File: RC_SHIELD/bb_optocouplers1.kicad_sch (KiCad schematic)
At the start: 40 parts, among them U1 SFH6345, U2 SFH6345, U6 SFH6345, U8 SFH6345

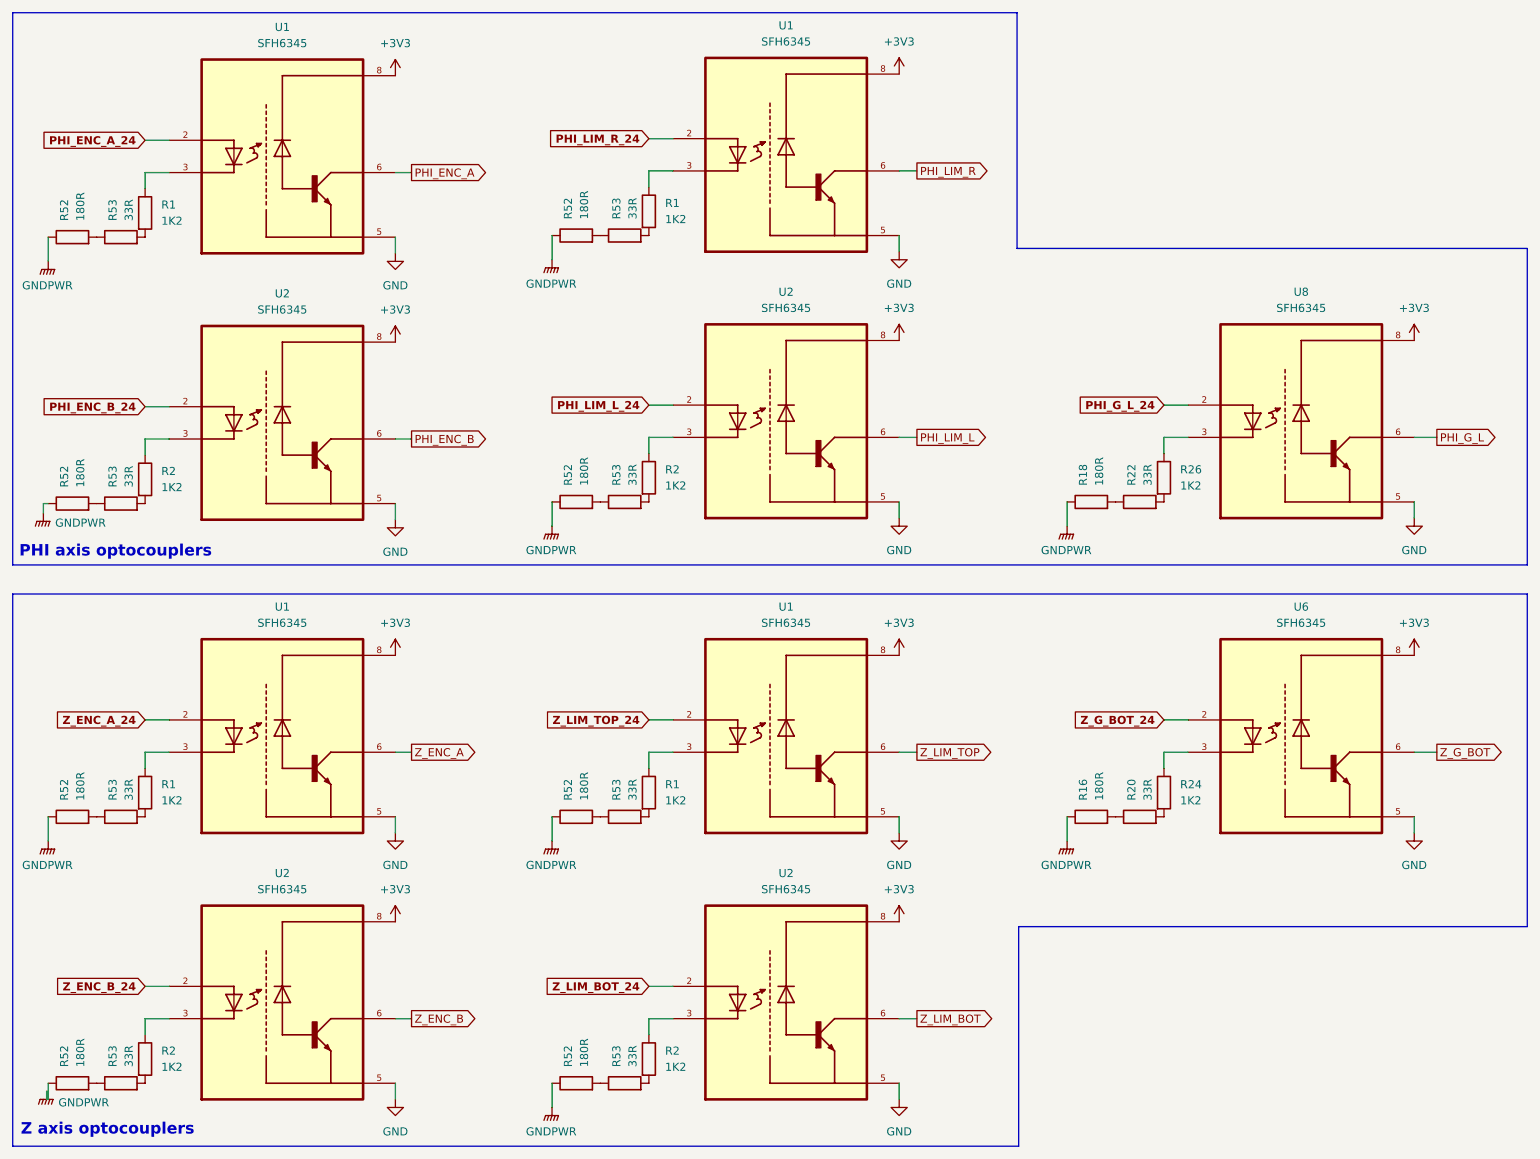
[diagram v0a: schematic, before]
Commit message: [SCH] reorganized optocouplers and tidied up page 2
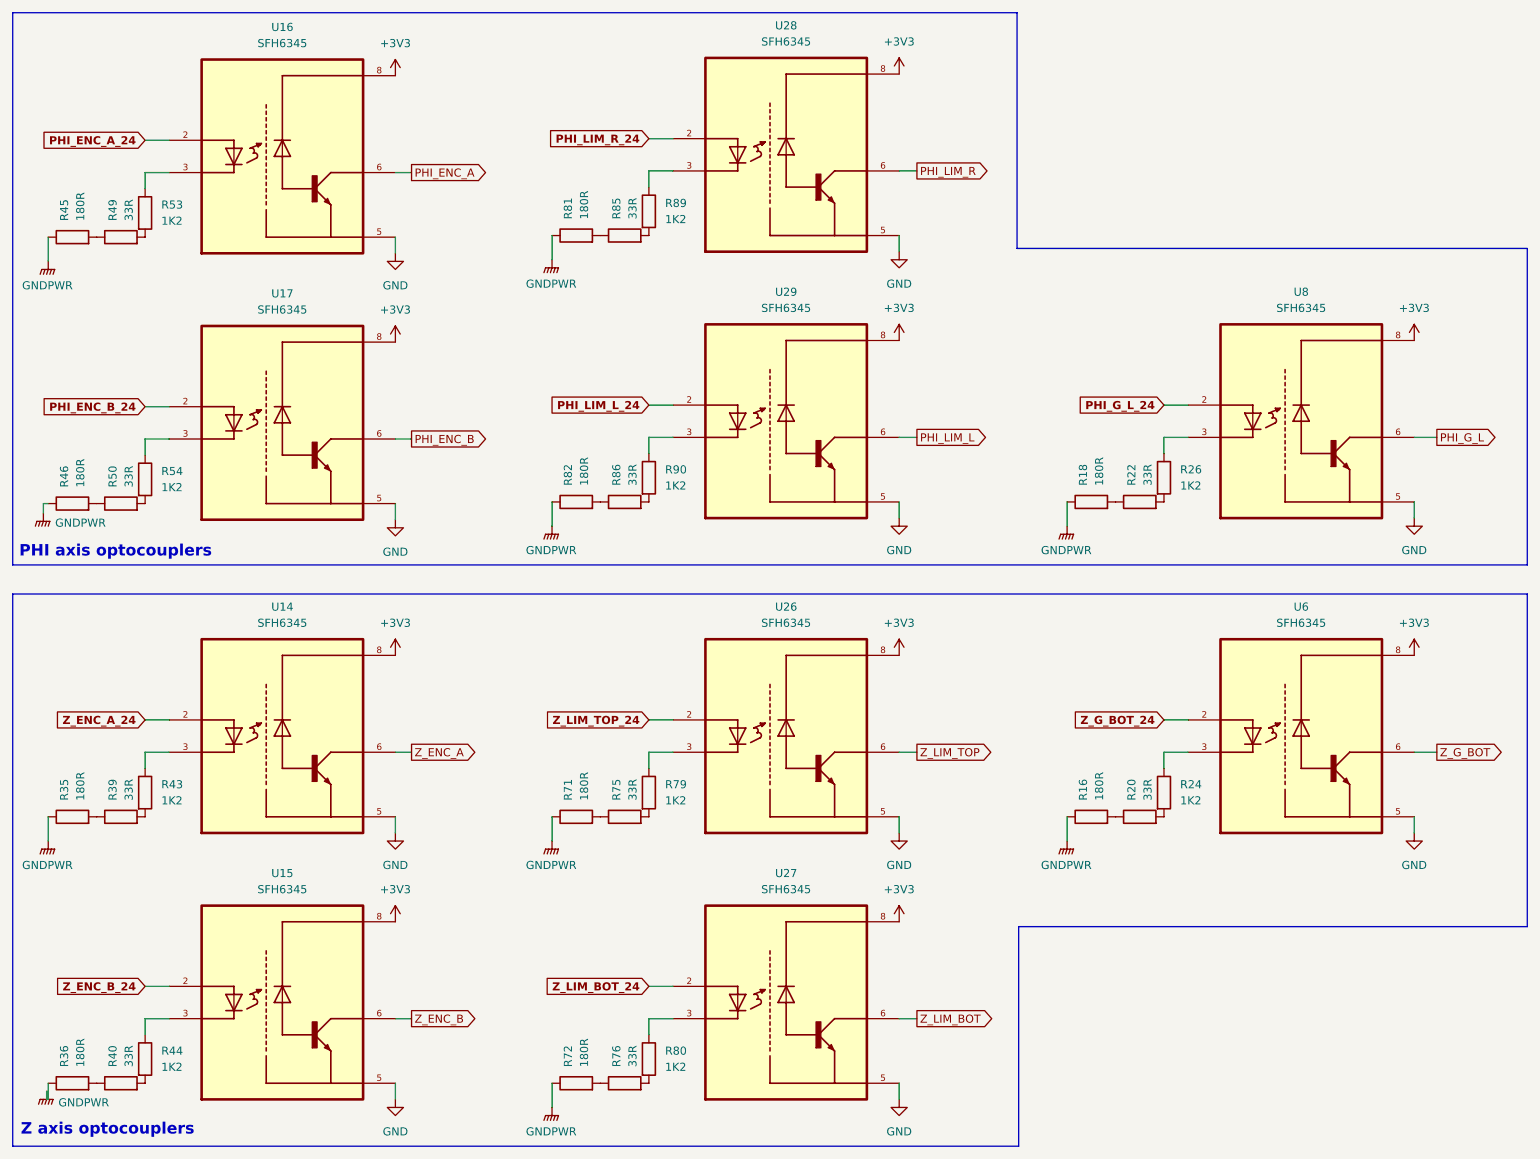
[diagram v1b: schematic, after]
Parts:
- renumbered R52 to R35, R52 to R36, R53 to R39, R53 to R40, R1 to R43, R2 to R44, R52 to R45, R52 to R46, R53 to R49, R53 to R50, R1 to R53, R2 to R54, R52 to R71, R52 to R72, R53 to R75, R53 to R76, R1 to R79, R2 to R80, R52 to R81, R52 to R82, R53 to R85, R53 to R86, R1 to R89, R2 to R90, U1 to U14, U2 to U15, U1 to U16, U2 to U17, U1 to U26, U2 to U27, U1 to U28, U2 to U29

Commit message: [SCH] reannotated entire schematic so PCBnew wont complain
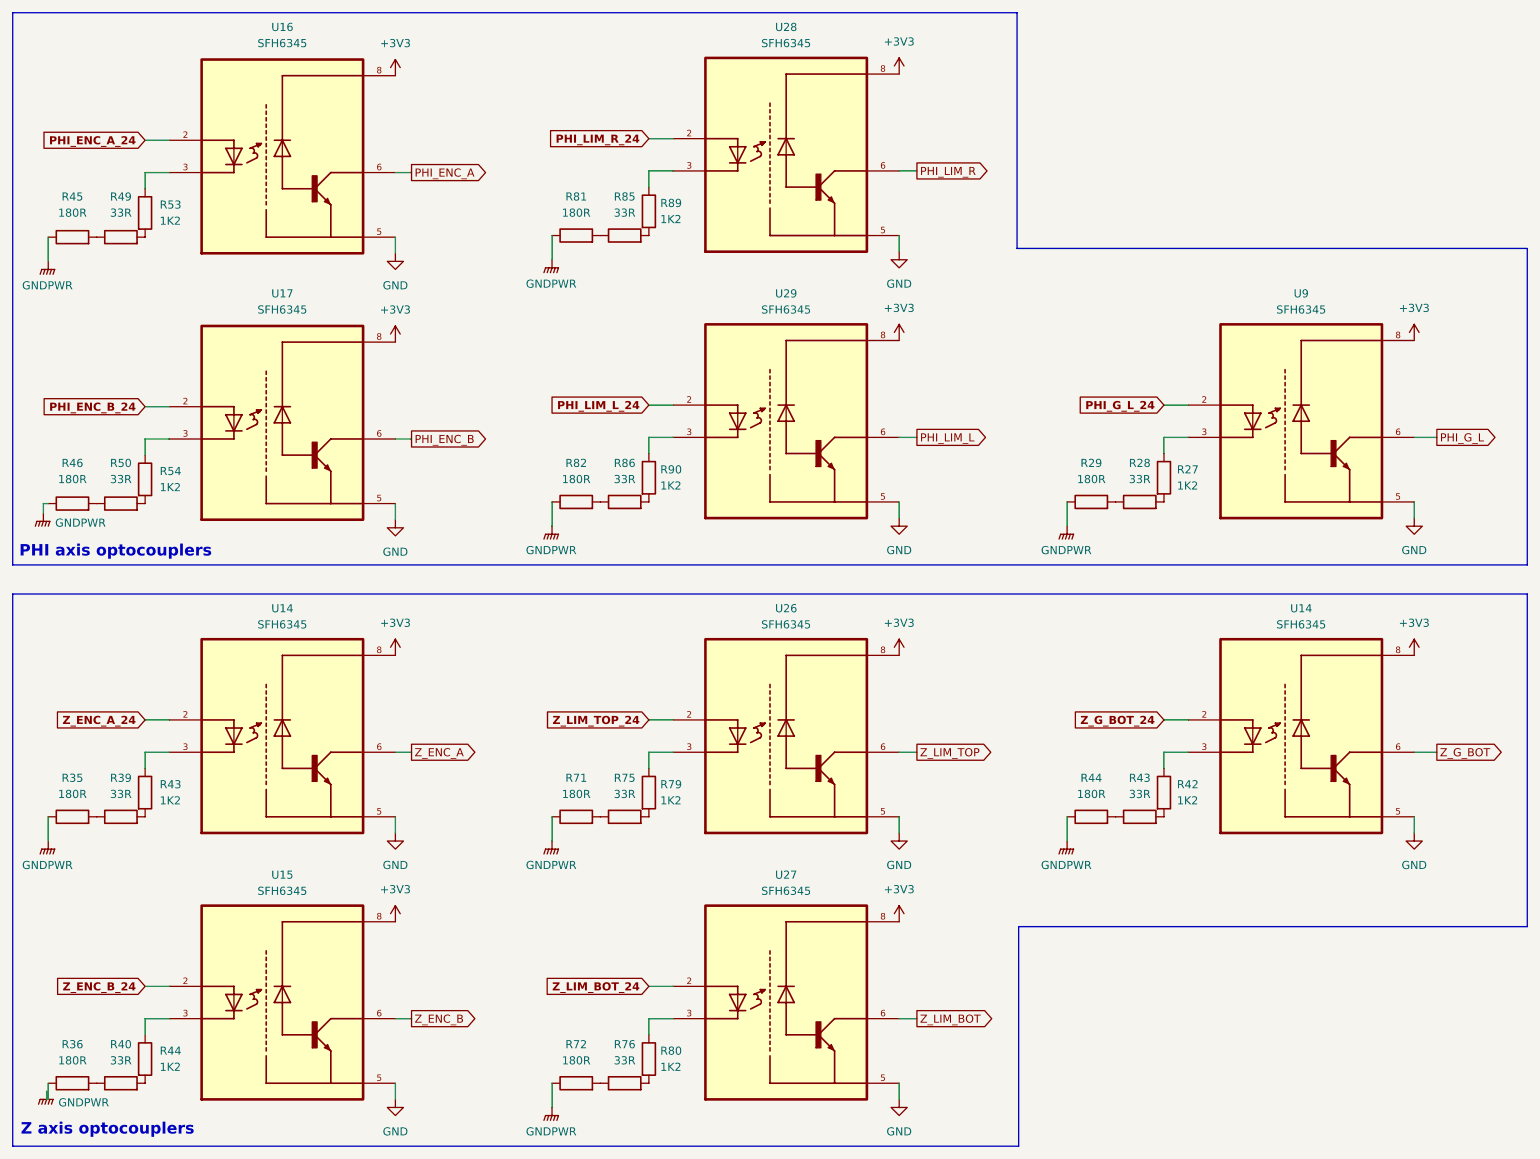
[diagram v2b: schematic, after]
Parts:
- renumbered R26 to R27, R22 to R28, R18 to R29, R24 to R42, R20 to R43, R16 to R44, U6 to U14, U8 to U9

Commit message: Revert "[SCH] reannotated entire schematic so PCBnew wont complain"
This reverts commit df148950bb8496d2d5af5a937770664cb0004a0d.
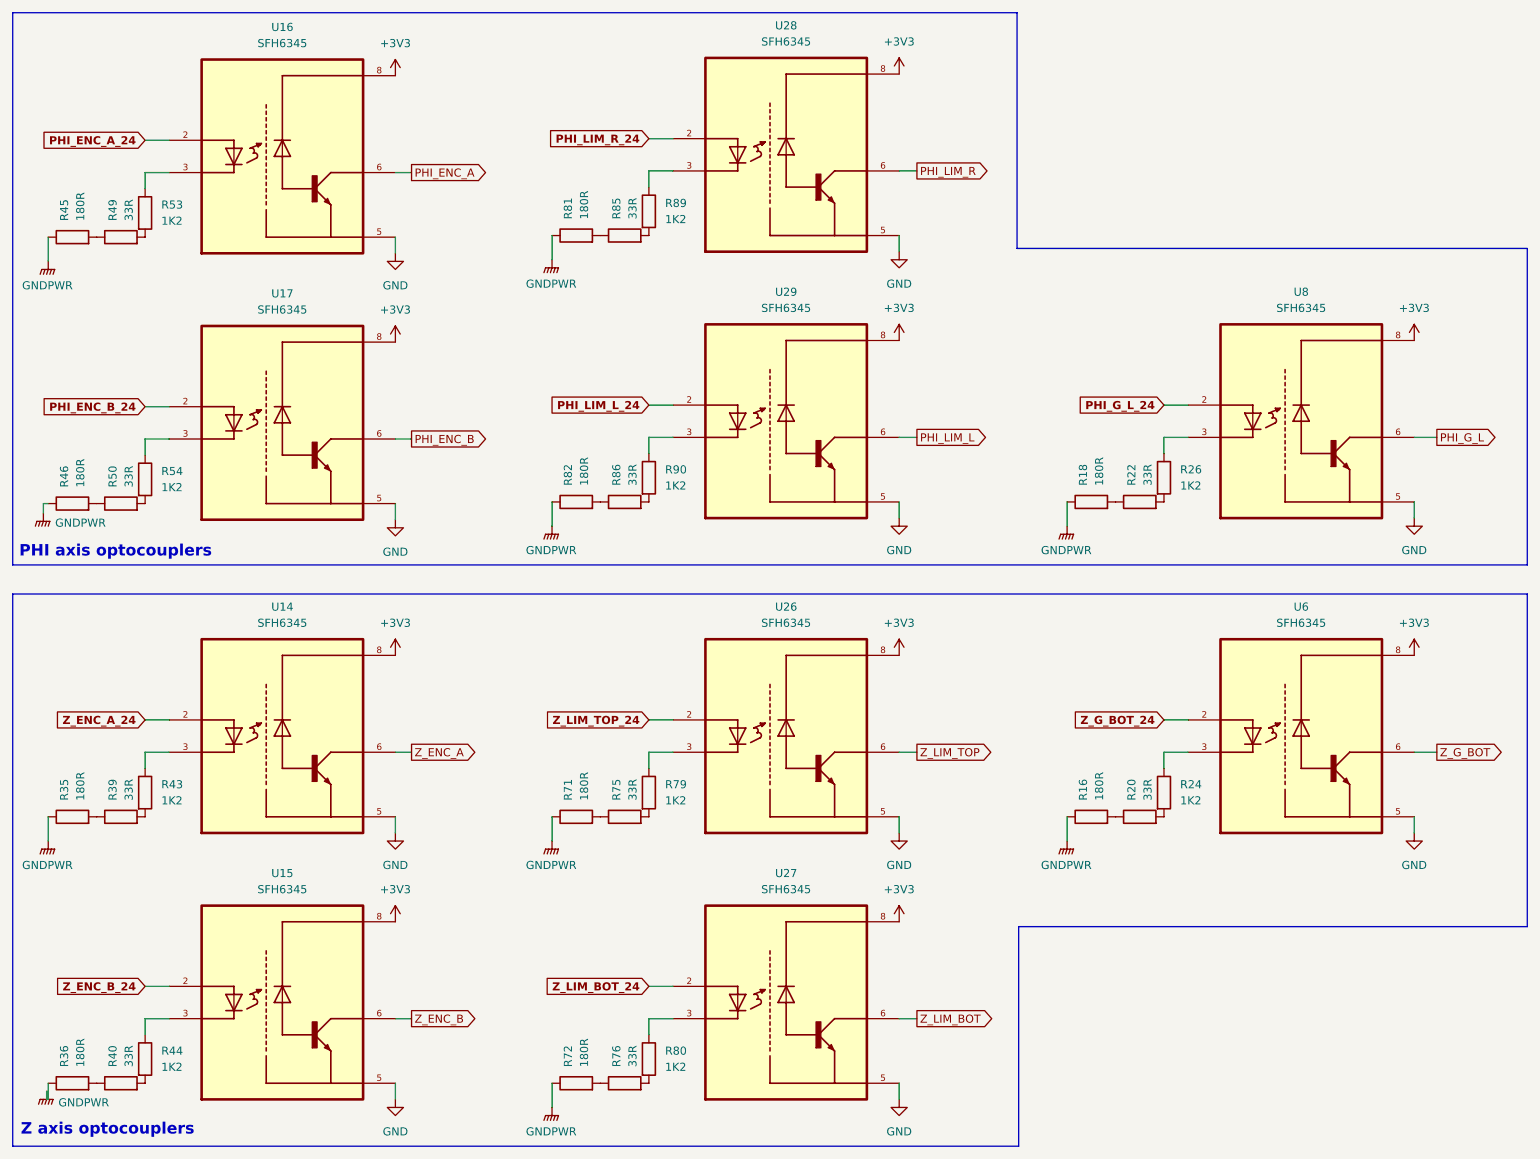
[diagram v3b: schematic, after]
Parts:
- renumbered R44 to R16, R29 to R18, R43 to R20, R28 to R22, R42 to R24, R27 to R26, U14 to U6, U9 to U8
